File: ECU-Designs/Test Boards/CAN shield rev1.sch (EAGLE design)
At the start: 22 parts

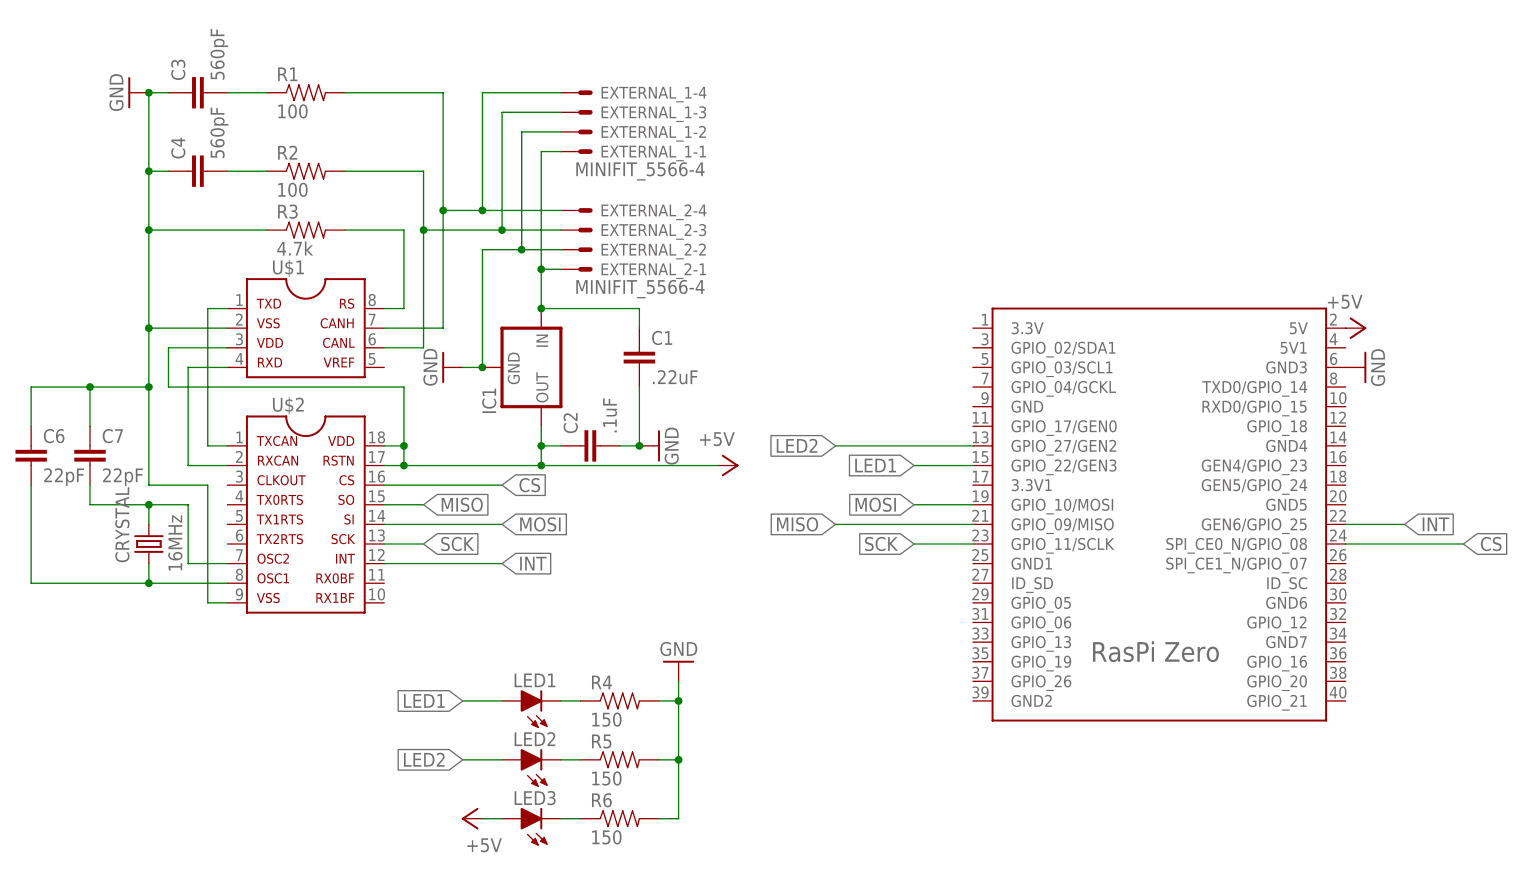
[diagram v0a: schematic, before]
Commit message: New versions of power board, bspd test board, can shield, bms adapter segment, bms shield
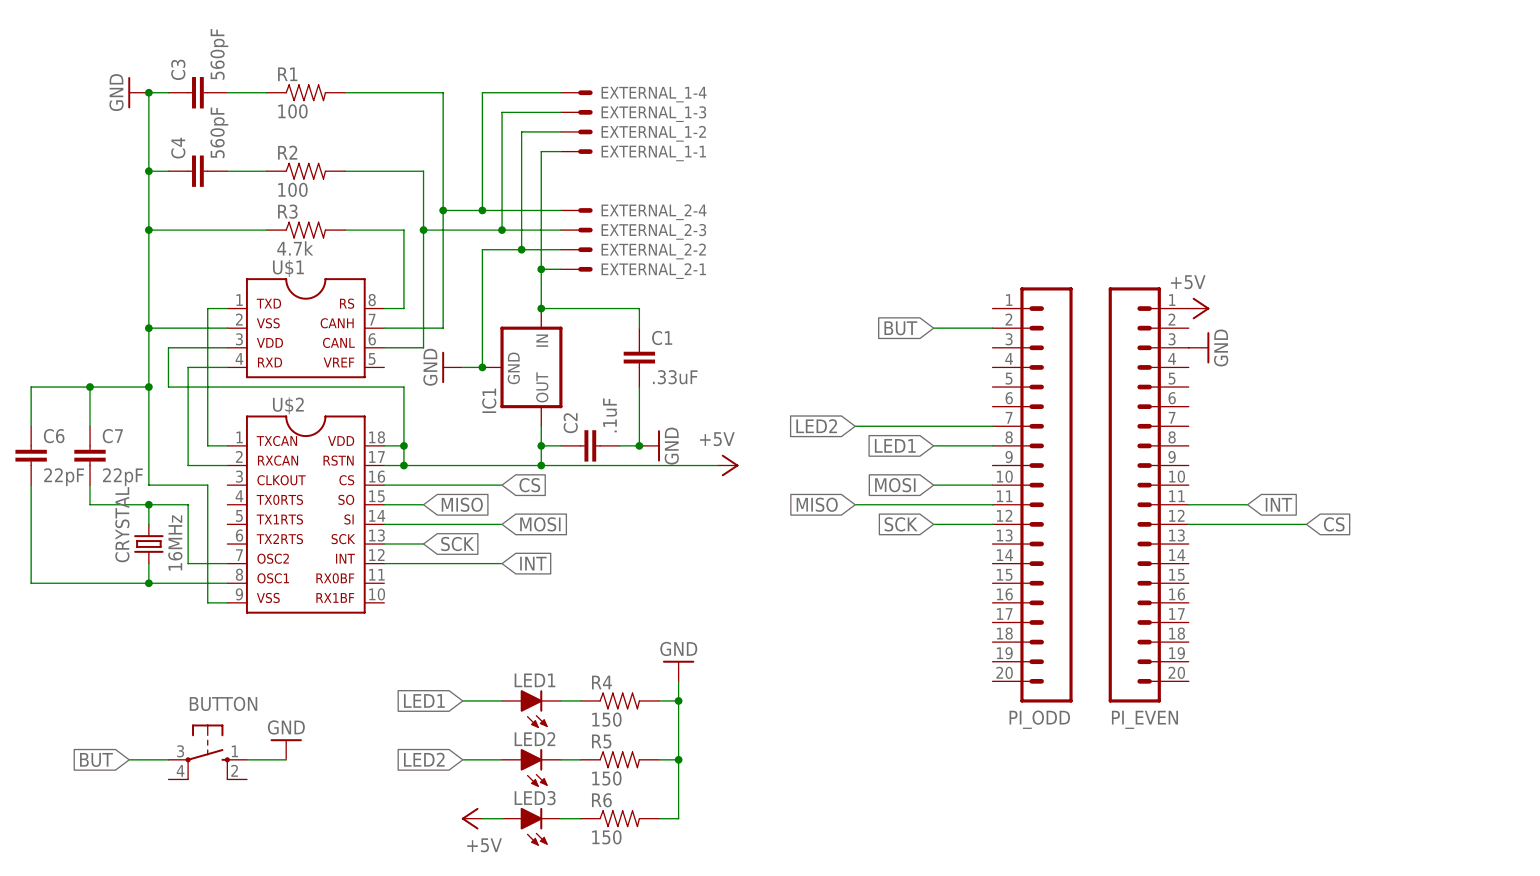
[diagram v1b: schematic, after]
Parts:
- removed U$3: RASPBERRY_PI_ZERO-V1.2, HyTechDevices:RASPBERRY_PI_ZERO-V1.2
- added BUTTON: (no value), HyTechDevices:BTN_10-XX
- added PI_EVEN, PI_ODD: (no value), HyTechDevices:M20
- C1: value .22uF -> .33uF
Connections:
- new net BUT: BUTTON.P, PI_ODD.2
- net +5V: now also PI_EVEN.1; no longer U$3.5V
- net CS: now also PI_EVEN.12; no longer U$3.SPI_CE0_N/GPIO_08
- net GND: now also BUTTON.S, PI_EVEN.3; no longer U$3.GND3
- net INT: now also PI_EVEN.11; no longer U$3.GEN6/GPIO_25
- net LED1: now also PI_ODD.8; no longer U$3.GPIO_22/GEN3
- net LED2: now also PI_ODD.7; no longer U$3.GPIO_27/GEN2
- net MISO: now also PI_ODD.11; no longer U$3.GPIO_09/MISO
- net MOSI: now also PI_ODD.10; no longer U$3.GPIO_10/MOSI
- net SCK: now also PI_ODD.12; no longer U$3.GPIO_11/SCLK
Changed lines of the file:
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@@
 <part name="CRYSTAL" library="SparkFun-FreqCtrl" deviceset="CRYSTAL" device="SMD" value="16MHz"/>
 <part name="GND4" library="HyTech 2016" deviceset="GND" device=""/>
-<part name="EXTERNAL_2" library="HyTechDevices" deviceset="MINIFIT_5566-4" device=""/>
+<part name="EXTERNAL_2" library="HyTechDevices" deviceset="MINIFIT_5566-4" device="" value=""/>
 <part name="U$1" library="HyTechDevices" deviceset="MCP2551" device=""/>
 <part name="U$2" library="HyTechDevices" deviceset="MCP2515" device="SMD"/>
 <part name="GND2" library="HyTech 2016" deviceset="GND" device=""/>
 <part name="GND1" library="HyTech 2016" deviceset="GND" device=""/>
-<part name="EXTERNAL_1" library="HyTechDevices" deviceset="MINIFIT_5566-4" device=""/>
+<part name="EXTERNAL_1" library="HyTechDevices" deviceset="MINIFIT_5566-4" device="" value=""/>
 <part name="GND5" library="HyTech 2016" deviceset="GND" device=""/>
 <part name="R1" library="HyTechDevices" deviceset="RESISTOR" device="0805-RES" value="100"/>
@@
 <part name="R3" library="HyTechDevices" deviceset="RESISTOR" device="0805-RES" value="4.7k"/>
 <part name="C2" library="HyTechDevices" deviceset="CAP" device="0805" value=".1uF"/>
-<part name="C1" library="HyTechDevices" deviceset="CAP" device="0805" value=".22uF"/>
+<part name="C1" library="HyTechDevices" deviceset="CAP" device="0805" value=".33uF"/>
 <part name="C3" library="HyTechDevices" deviceset="CAP" device="0805" value="560pF"/>
 <part name="C4" library="HyTechDevices" deviceset="CAP" device="0805" value="560pF"/>
@@
 <part name="R6" library="HyTechDevices" deviceset="RESISTOR" device="0805-RES" value="150"/>
 <part name="IC1" library="HyTechDevices" deviceset="5VREG_L7805" device="_HOR"/>
-<part name="U$3" library="HyTechDevices" deviceset="RASPBERRY_PI_ZERO-V1.2" device=""/>
 <part name="P+1" library="supply1" deviceset="+5V" device=""/>
-<part name="P+2" library="supply1" deviceset="+5V" device=""/>
-<part name="GND6" library="HyTech 2016" deviceset="GND" device=""/>
 <part name="P+3" library="supply1" deviceset="+5V" device=""/>
 <part name="LED2" library="HyTechDevices" deviceset="LED" device="-0805"/>
 <part name="R5" library="HyTechDevices" deviceset="RESISTOR" device="0805-RES" value="150"/>
+<part name="PI_EVEN" library="HyTechDevices" deviceset="M20" device=""/>
+<part name="PI_ODD" library="HyTechDevices" deviceset="M20" device=""/>
+<part name="P+4" library="supply1" deviceset="+5V" device=""/>
+<part name="GND3" library="HyTech 2016" deviceset="GND" device=""/>
+<part name="BUTTON" library="HyTechDevices" deviceset="BTN_10-XX" device=""/>
+<part name="GND6" library="HyTech 2016" deviceset="GND" device=""/>
 </parts>
 <sheets>
@@
 <instance part="R6" gate="G$1" x="134.62" y="-17.78"/>
 <instance part="IC1" gate="G$1" x="124.46" y="40.64" rot="R270"/>
-<instance part="U$3" gate="G$1" x="203.2" y="15.24"/>
 <instance part="P+1" gate="1" x="149.86" y="27.94" rot="R270"/>
-<instance part="P+2" gate="1" x="231.14" y="45.72" rot="R270"/>
-<instance part="GND6" gate="1" x="231.14" y="40.64" rot="R90"/>
 <instance part="P+3" gate="1" x="114.3" y="-17.78" rot="R90"/>
 <instance part="LED2" gate="LED" x="121.92" y="-10.16" rot="R90"/>
 <instance part="R5" gate="G$1" x="134.62" y="-10.16"/>
+<instance part="PI_EVEN" gate="G$1" x="198.12" y="53.34" rot="MR180"/>
+<instance part="PI_ODD" gate="G$1" x="193.04" y="53.34" rot="R180"/>
+<instance part="P+4" gate="1" x="210.82" y="48.26" rot="R270"/>
+<instance part="GND3" gate="1" x="210.82" y="43.18" rot="R90"/>
+<instance part="BUTTON" gate="1" x="81.28" y="-10.16" rot="R270"/>
+<instance part="GND6" gate="1" x="91.44" y="-7.62" rot="R180"/>
 </instances>
 <busses>
@@
 </segment>
 <segment>
-<pinref part="U$3" gate="G$1" pin="GND3"/>
+<pinref part="GND3" gate="1" pin="GND"/>
+<pinref part="PI_EVEN" gate="G$1" pin="3"/>
+</segment>
+<segment>
 <pinref part="GND6" gate="1" pin="GND"/>
+<pinref part="BUTTON" gate="1" pin="S"/>
+<wire x1="91.44" y1="-10.16" x2="86.36" y2="-10.16" width="0.1524" layer="91"/>
 </segment>
 </net>
@@
 <net name="CS" class="0">
 <segment>
-<pinref part="U$3" gate="G$1" pin="SPI_CE0_N/GPIO_08"/>
-<wire x1="228.6" y1="17.78" x2="243.84" y2="17.78" width="0.1524" layer="91"/>
-<label x="243.84" y="17.78" size="1.778" layer="95" xref="yes"/>
-</segment>
-<segment>
 <pinref part="U$2" gate="G$1" pin="16"/>
 <wire x1="104.14" y1="25.4" x2="119.38" y2="25.4" width="0.1524" layer="91"/>
 <label x="119.38" y="25.4" size="1.778" layer="95" xref="yes"/>
 </segment>
+<segment>
+<wire x1="208.28" y1="20.32" x2="223.52" y2="20.32" width="0.1524" layer="91"/>
+<label x="223.52" y="20.32" size="1.778" layer="95" xref="yes"/>
+<pinref part="PI_EVEN" gate="G$1" pin="12"/>
+</segment>
 </net>
 <net name="MISO" class="0">
@@
 </segment>
 <segment>
-<pinref part="U$3" gate="G$1" pin="GPIO_09/MISO"/>
-<wire x1="180.34" y1="20.32" x2="162.56" y2="20.32" width="0.1524" layer="91"/>
-<label x="162.56" y="20.32" size="1.778" layer="95" rot="R180" xref="yes"/>
+<wire x1="182.88" y1="22.86" x2="165.1" y2="22.86" width="0.1524" layer="91"/>
+<label x="165.1" y="22.86" size="1.778" layer="95" rot="R180" xref="yes"/>
+<pinref part="PI_ODD" gate="G$1" pin="11"/>
 </segment>
 </net>
@@
 </segment>
 <segment>
-<pinref part="U$3" gate="G$1" pin="GPIO_10/MOSI"/>
-<wire x1="180.34" y1="22.86" x2="172.72" y2="22.86" width="0.1524" layer="91"/>
-<label x="172.72" y="22.86" size="1.778" layer="95" rot="R180" xref="yes"/>
+<wire x1="182.88" y1="25.4" x2="175.26" y2="25.4" width="0.1524" layer="91"/>
+<label x="175.26" y="25.4" size="1.778" layer="95" rot="R180" xref="yes"/>
+<pinref part="PI_ODD" gate="G$1" pin="10"/>
 </segment>
 </net>
@@
 </segment>
 <segment>
-<pinref part="U$3" gate="G$1" pin="GPIO_11/SCLK"/>
-<wire x1="180.34" y1="17.78" x2="172.72" y2="17.78" width="0.1524" layer="91"/>
-<label x="172.72" y="17.78" size="1.778" layer="95" rot="R180" xref="yes"/>
+<wire x1="182.88" y1="20.32" x2="175.26" y2="20.32" width="0.1524" layer="91"/>
+<label x="175.26" y="20.32" size="1.778" layer="95" rot="R180" xref="yes"/>
+<pinref part="PI_ODD" gate="G$1" pin="12"/>
 </segment>
 </net>
@@
 </segment>
 <segment>
-<pinref part="U$3" gate="G$1" pin="GEN6/GPIO_25"/>
-<wire x1="228.6" y1="20.32" x2="236.22" y2="20.32" width="0.1524" layer="91"/>
-<label x="236.22" y="20.32" size="1.778" layer="95" xref="yes"/>
+<wire x1="208.28" y1="22.86" x2="215.9" y2="22.86" width="0.1524" layer="91"/>
+<label x="215.9" y="22.86" size="1.778" layer="95" xref="yes"/>
+<pinref part="PI_EVEN" gate="G$1" pin="11"/>
 </segment>
 </net>
@@
 </segment>
 <segment>
-<pinref part="U$3" gate="G$1" pin="5V"/>
-<pinref part="P+2" gate="1" pin="+5V"/>
+<pinref part="P+4" gate="1" pin="+5V"/>
+<pinref part="PI_EVEN" gate="G$1" pin="1"/>
 </segment>
 </net>
 <net name="LED2" class="0">
-<segment>
-<pinref part="U$3" gate="G$1" pin="GPIO_27/GEN2"/>
-<wire x1="180.34" y1="30.48" x2="162.56" y2="30.48" width="0.1524" layer="91"/>
-<label x="162.56" y="30.48" size="1.778" layer="95" rot="R180" xref="yes"/>
-</segment>
 <segment>
 <pinref part="LED2" gate="LED" pin="A"/>
@@
 <label x="114.3" y="-10.16" size="1.778" layer="95" rot="R180" xref="yes"/>
 </segment>
+<segment>
+<wire x1="182.88" y1="33.02" x2="165.1" y2="33.02" width="0.1524" layer="91"/>
+<label x="165.1" y="33.02" size="1.778" layer="95" rot="R180" xref="yes"/>
+<pinref part="PI_ODD" gate="G$1" pin="7"/>
+</segment>
 </net>
 <net name="LED1" class="0">
-<segment>
-<pinref part="U$3" gate="G$1" pin="GPIO_22/GEN3"/>
-<wire x1="180.34" y1="27.94" x2="172.72" y2="27.94" width="0.1524" layer="91"/>
-<label x="172.72" y="27.94" size="1.778" layer="95" rot="R180" xref="yes"/>
-</segment>
 <segment>
 <pinref part="LED1" gate="LED" pin="A"/>
@@
 <label x="114.3" y="-2.54" size="1.778" layer="95" rot="R180" xref="yes"/>
 </segment>
+<segment>
+<wire x1="182.88" y1="30.48" x2="175.26" y2="30.48" width="0.1524" layer="91"/>
+<label x="175.26" y="30.48" size="1.778" layer="95" rot="R180" xref="yes"/>
+<pinref part="PI_ODD" gate="G$1" pin="8"/>
+</segment>
 </net>
 <net name="N$2" class="0">
@@
 </segment>
 </net>
+<net name="BUT" class="0">
+<segment>
+<pinref part="PI_ODD" gate="G$1" pin="2"/>
+<wire x1="182.88" y1="45.72" x2="175.26" y2="45.72" width="0.1524" layer="91"/>
+<label x="175.26" y="45.72" size="1.778" layer="95" rot="R180" xref="yes"/>
+</segment>
+<segment>
+<pinref part="BUTTON" gate="1" pin="P"/>
+<wire x1="76.2" y1="-10.16" x2="71.12" y2="-10.16" width="0.1524" layer="91"/>
+<label x="71.12" y="-10.16" size="1.778" layer="95" rot="R180" xref="yes"/>
+</segment>
+</net>
